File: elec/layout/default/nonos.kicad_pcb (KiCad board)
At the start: 2 copper layers, 45 x 122 mm, 73 parts, among them CN1 HRSHirose_DF40C_100DS_0_4V51, CN2 HRSHirose_DF40C_100DS_0_4V51, Q1 MOSFET, U1 STUSB4500QTR, U2 _Texas_Instruments_SN74LVC1G0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, U3 _Texas_Instruments_TAS5825MRH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, U4 _HCTL_HC_TYPE_C_24P_VS9_3_5A_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, U5 JST_Sales_America_B02B_XASK_1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, U6 JST_Sales_America_B02B_XASK_1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, U7 _Texas_Instruments_TPS56637RP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

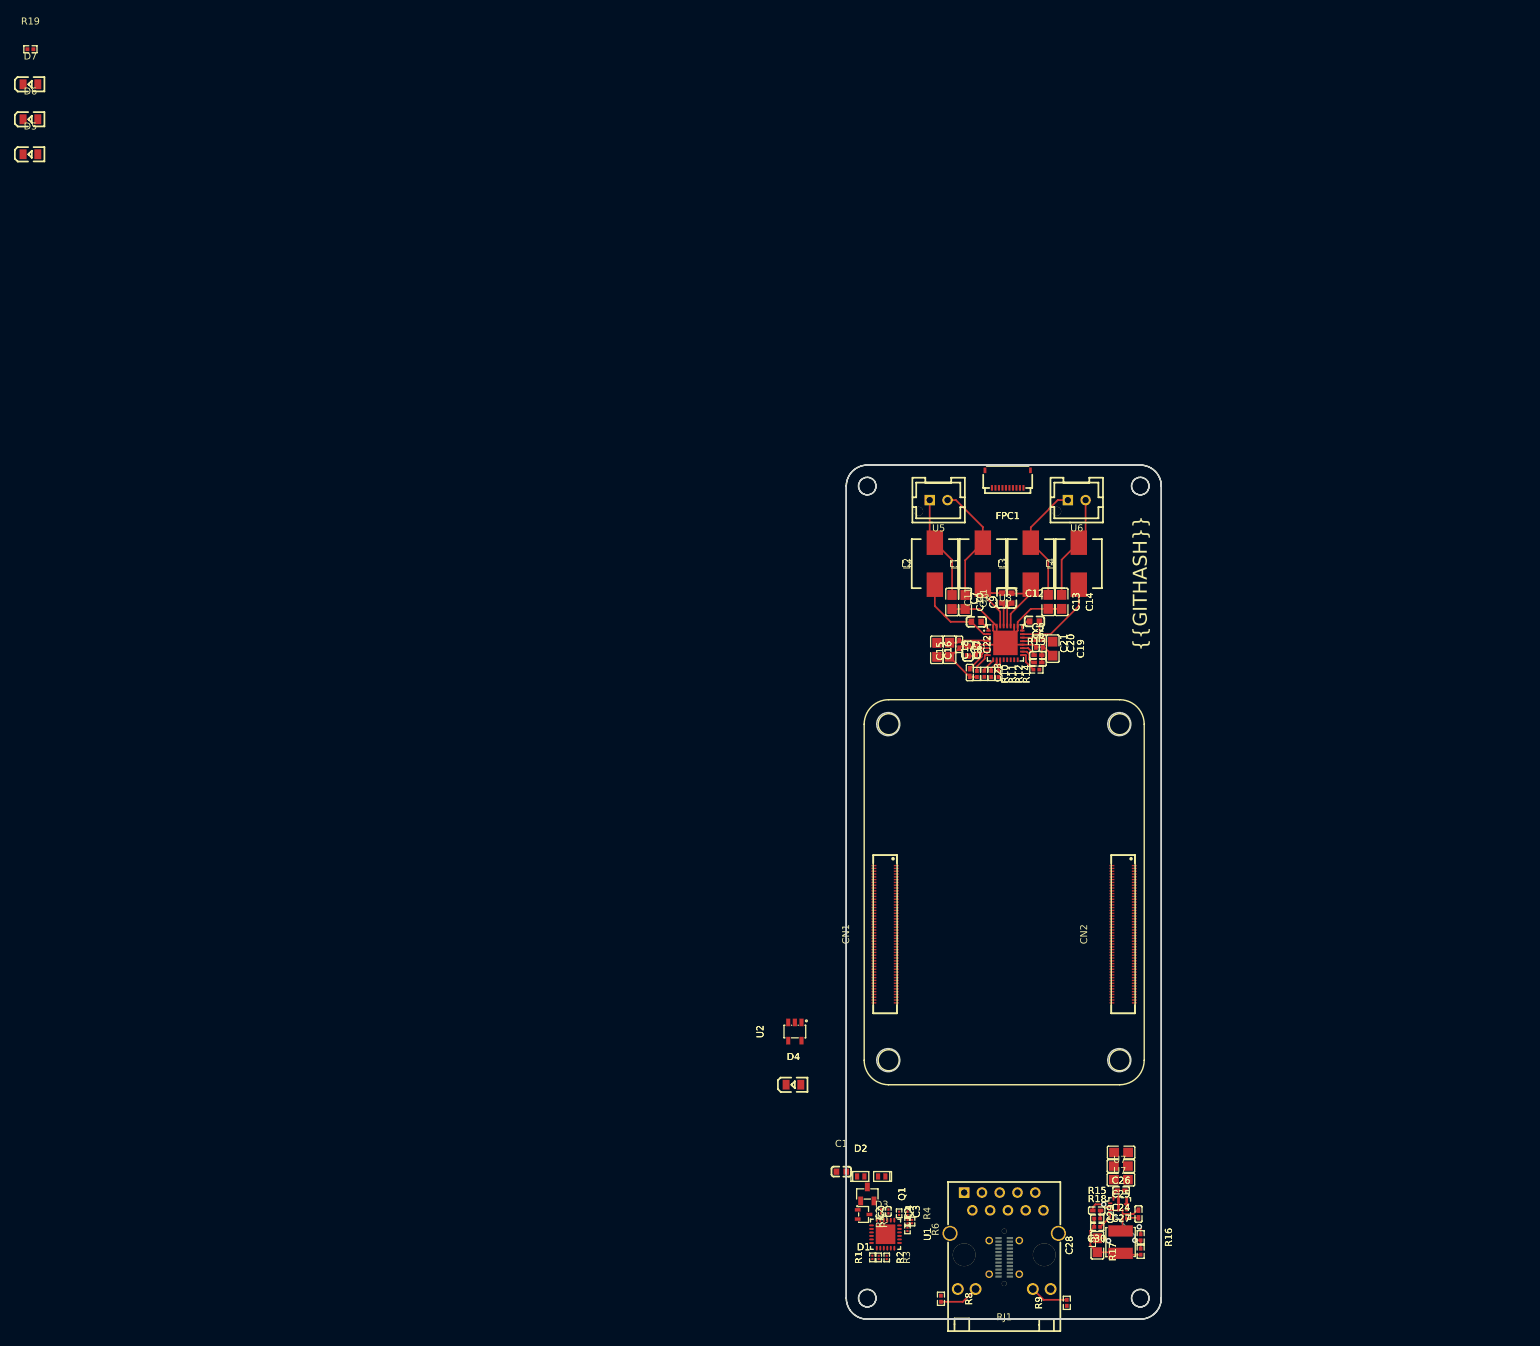
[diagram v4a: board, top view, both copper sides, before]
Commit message: fixed hat-footprint
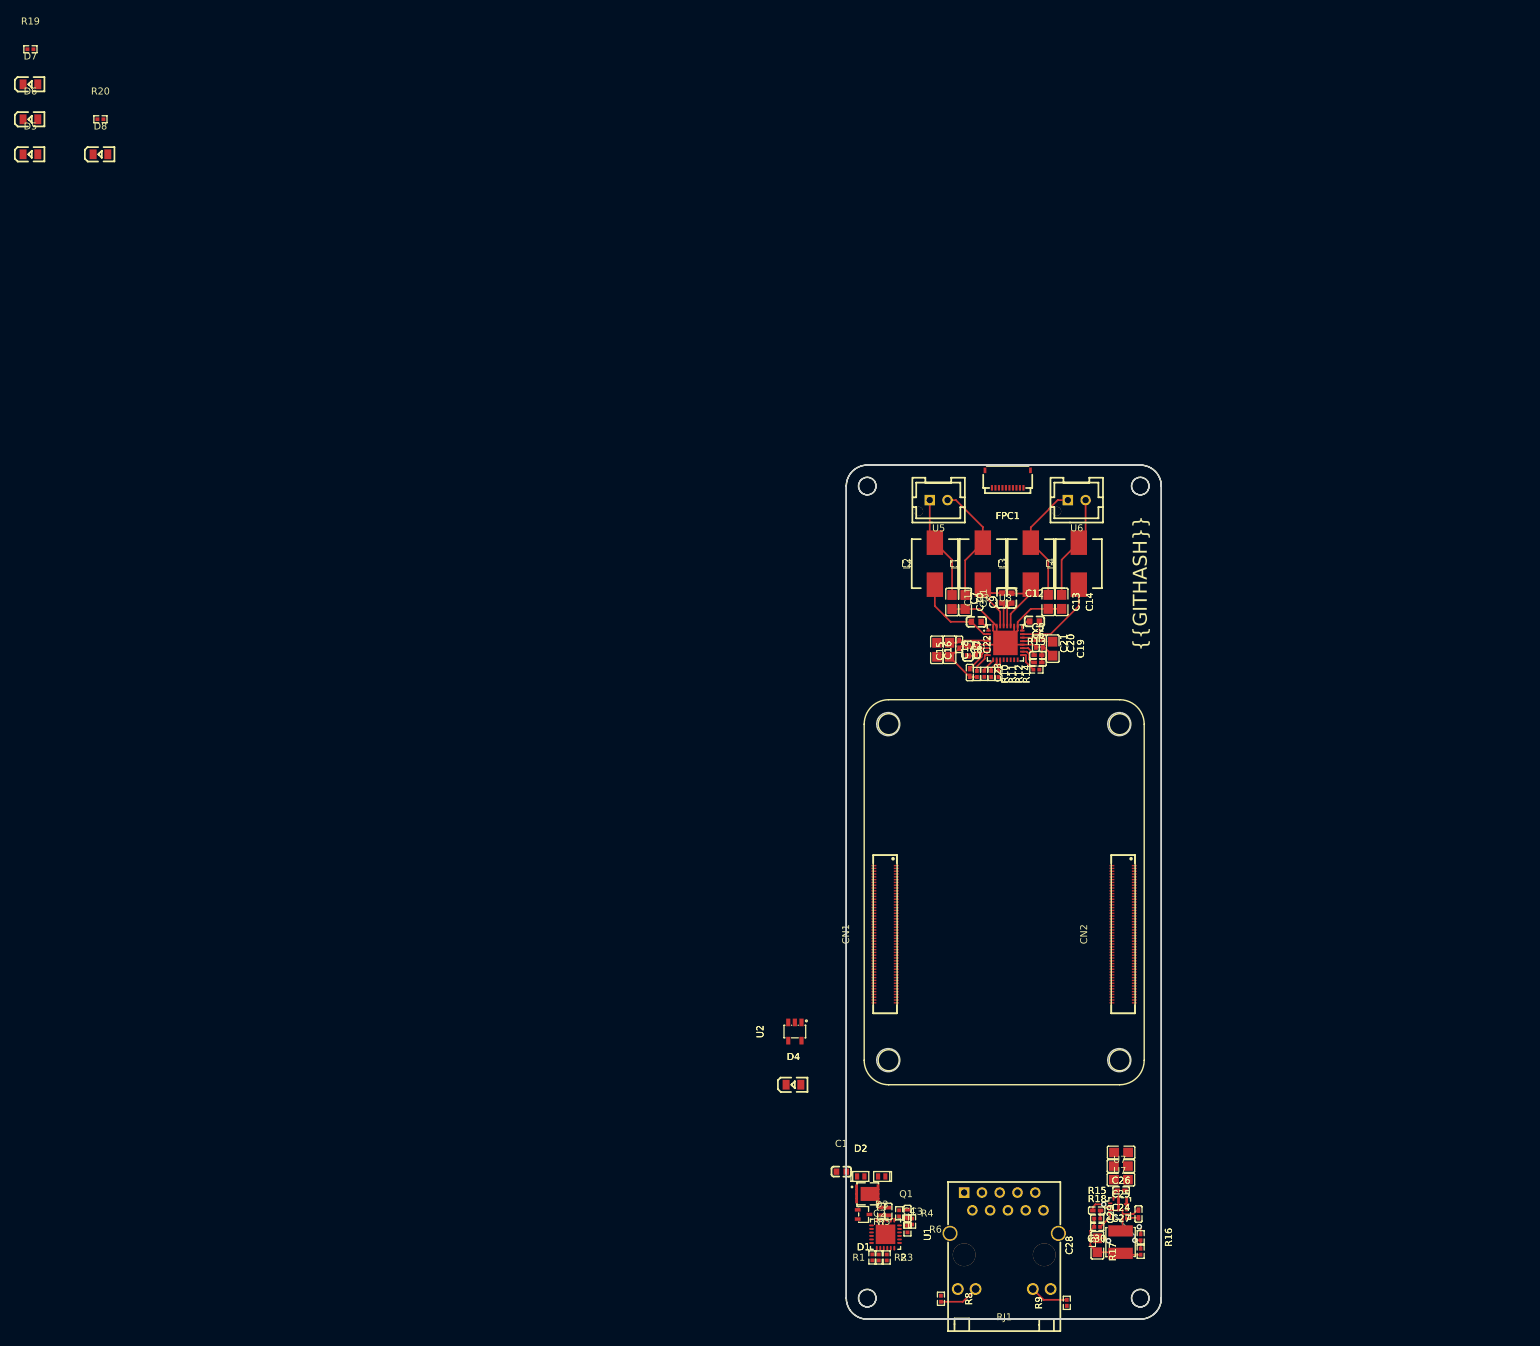
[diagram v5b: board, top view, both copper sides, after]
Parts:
- removed U4: _HCTL_HC_TYPE_C_24P_VS9_3_5A_F1_1_04, lcsc:USB-C-SMD_HC-TYPE-C-24P-VS9.3-5A-F1.1-04
- added D8: , lcsc:LED0805-R-RD, F.Cu at (10.0, 0.00)
- added R20: 5.1kΩ ±1% 62.5mW, lcsc:R0402, F.Cu at (10.0, -5.00)
- C2: value 100nF ±10% 10V X5R -> 100nF ±10% 16V X7R; footprint lcsc:C0201 -> lcsc:C0402
- C3, C4: value 1µF ±20% 6.3V X5R -> 1µF ±10% 25V X5R; footprint lcsc:C0201 -> lcsc:C0402
- Q1: footprint lcsc:SOT-23-3_L2.9-W1.3-P1.90-LS2.4-BR-1 -> lcsc:PDFN3333-8_L3.1-W3.2-P0.65-LS3.4-BL
- R1, R4: value 1kΩ ±1% 50mW -> 1kΩ ±1% 62.5mW; footprint lcsc:R0201 -> lcsc:R0402
- R2, R3: value 4.7kΩ ±1% 50mW -> 4.7kΩ ±1% 62.5mW; footprint lcsc:R0201 -> lcsc:R0402
- R5: value 100kΩ ±1% 50mW -> 100kΩ ±1% 62.5mW; footprint lcsc:R0201 -> lcsc:R0402
- R6: value 22.1kΩ ±1% 50mW -> 22kΩ ±1% 62.5mW; footprint lcsc:R0201 -> lcsc:R0402
- R7: value 100Ω ±1% 50mW -> 100Ω ±1% 62.5mW; footprint lcsc:R0201 -> lcsc:R0402
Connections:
- net pins[26] renamed processor.hdi_b-pins[26]
- net pins[28] renamed processor.hdi_b-pins[28]
- net pins[30] renamed processor-signal-9
- net pins[44] renamed processor-pins[44]-1
- net processor-pins[46]-1 renamed pins[46]
- net processor.hdi_b-pins[27] renamed pins[27]
- net processor.hdi_b-pins[38] renamed pins[38]
- C11 pad 1: amplifier-net-6 -> amplifier-net-11
- C11 pad 2: amplifier-net-4 -> amplifier-net-2
- C12 pad 2: amplifier-net-3 -> amplifier-net-6
- C14 pad 1: net-2 -> net-1
- C2 pad 1: pd_controller-net-2 -> pd_controller-net-1
- C23 pad 1: amplifier-net-8 -> amplifier-net-4
- C30 pad 1: regulator-net-4 -> regulator-net-1
- C5 pad 1: amplifier-net-7 -> amplifier-net-8
- C6 pad 1: amplifier-net-9 -> amplifier-net-7
- C7 pad 2: amplifier-net-2 -> amplifier-net-9
- C8 pad 1: amplifier-net -> amplifier-net-1
- C8 pad 2: amplifier-net-1 -> amplifier-net
- C9 pad 1: net-1 -> net-2
- CN1 pad 14: processor-pins[27] -> processor-signal-7
- CN1 pad 17: signal-3 -> signal-2
- CN1 pad 19: processor-signal-5 -> pins[37]
- CN1 pad 23: processor-signal -> processor-signal-2
- CN1 pad 24: processor-signal-7 -> processor-signal-5
- CN1 pad 25: processor-signal-3 -> processor-signal-8
- CN1 pad 28: signal-5 -> signal
- CN1 pad 29: signal-6 -> signal-7
- CN1 pad 73: processor-signal-1 -> processor-signal-3
- CN1 pad 75: pins[50] -> processor-signal-4
- CN1 pad 77: processor-pins[46] -> processor-signal-6
- CN1 pad 78: processor-signal-4 -> processor-pins[44]
- CN1 pad 80: processor-signal-8 -> processor-signal
- CN1 pad 81: processor-pins[38] -> processor-signal-1
- CN1 pad 82: signal-2 -> signal-3
- CN1 pad 86: processor-signal-6 -> processor-pins[28]
- CN1 pad 87: processor-signal-2 -> processor-pins[26]
- D4 pad 1: processor-net -> processor-net-2
- D4 pad 2: processor-net-1 -> processor-net
- D5 pad 2: cathode -> cathode-2
- D6 pad 2: cathode-1 -> cathode
- D7 pad 2: cathode-2 -> cathode-1
- FPC1 pad 10: signal-2 -> signal-3
- FPC1 pad 8: signal-3 -> signal-2
- L1 pad 1: amplifier-net-2 -> amplifier-net-9
- L1 pad 2: net-1 -> net-2
- L2 pad 1: amplifier-net-1 -> amplifier-net
- L3 pad 1: amplifier-net-4 -> amplifier-net-2
- L4 pad 1: amplifier-net-3 -> amplifier-net-6
- L4 pad 2: net-2 -> net-1
- Q1 pad 1: pd_controller-net -> pd_controller.VSINK_MOSFET.footprint.pins[0].net-net
- Q1 pad 2: VBUS -> pd_controller.VSINK_MOSFET.footprint.pins[1].net-net
- Q1 pad 3: VSINK_VCC -> VBUS
- R1 pad 2: pd_controller-net-4 -> pd_controller-net-3
- R10 pad 1: amplifier-net-11 -> amplifier-net-3
- R11 pad 1: signal-6 -> signal-7
- R12 pad 1: signal-7 -> signal-5
- R13 pad 1: signal-5 -> signal
- R14 pad 1: signal -> signal-6
- R15 pad 2: regulator-net-4 -> regulator-net-1
- R18 pad 2: regulator-net-1 -> regulator-net-4
- R19 pad 1: processor-net-1 -> processor-net
- R4 pad 2: pd_controller-net-1 -> pd_controller-net-2
- R6 pad 2: pd_controller-net-3 -> pd_controller-net-4
- R7 pad 2: pd_controller-net-2 -> pd_controller-net-1
- R8 pad 2: rj45-net-1 -> rj45-net
- R9 pad 2: rj45-net -> rj45-net-1
- RJ1 pad 12: rj45-net-1 -> rj45-net
- RJ1 pad 13: rj45-net -> rj45-net-1
- U1 pad 1: CC1 -> pd_controller.PD_CONTROLLER-signal
- U1 pad 16: pd_controller-net-3 -> pd_controller-net-4
- U1 pad 18: pd_controller-net-1 -> pd_controller-net-2
- U1 pad 5: CC2 -> pd_controller.PD_CONTROLLER-signal-1
- U1 pad 9: pd_controller-net-4 -> pd_controller-net-3
- U2 pad 4: processor-net -> processor-net-2
- U3 pad 1: amplifier-net -> amplifier-net-1
- U3 pad 10: signal-7 -> signal-5
- U3 pad 11: signal -> signal-6
- U3 pad 17: signal-5 -> signal
- U3 pad 18: amplifier-net-9 -> amplifier-net-7
- U3 pad 19: amplifier-net-7 -> amplifier-net-8
- U3 pad 2: amplifier-net-1 -> amplifier-net
- U3 pad 23: amplifier-net-3 -> amplifier-net-6
- U3 pad 27: amplifier-net-4 -> amplifier-net-2
- U3 pad 28: amplifier-net-6 -> amplifier-net-11
- U3 pad 30: amplifier-net-2 -> amplifier-net-9
- U3 pad 7: amplifier-net-8 -> amplifier-net-4
- U3 pad 8: amplifier-net-11 -> amplifier-net-3
- U3 pad 9: signal-6 -> signal-7
- U5 pad 2: net-1 -> net-2
- U6 pad 2: net-2 -> net-1
- U7 pad 4: regulator-net-1 -> regulator-net-4
